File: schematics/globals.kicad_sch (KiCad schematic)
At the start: 20 parts, among them J1 Power, SW1 SW_Push, U1 74HC04, U12 74HC04, U2 NE555P, Y1 4MHz

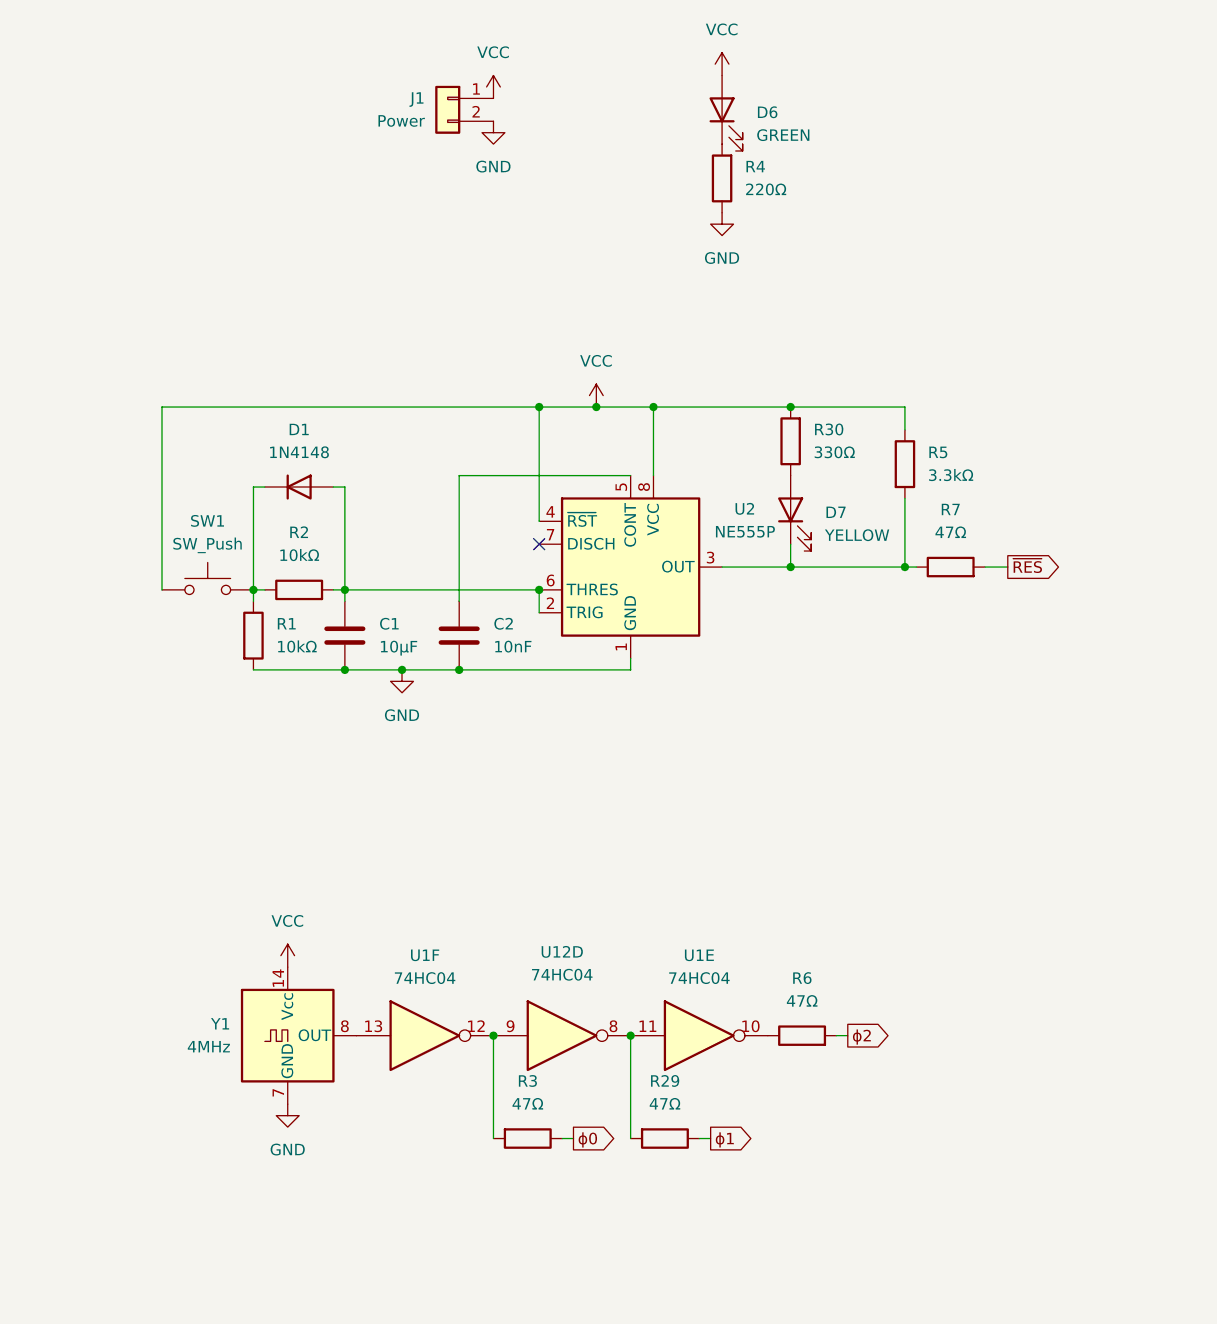
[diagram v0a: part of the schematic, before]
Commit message: trying to make it automatically hold reset during power-on. it's a little better
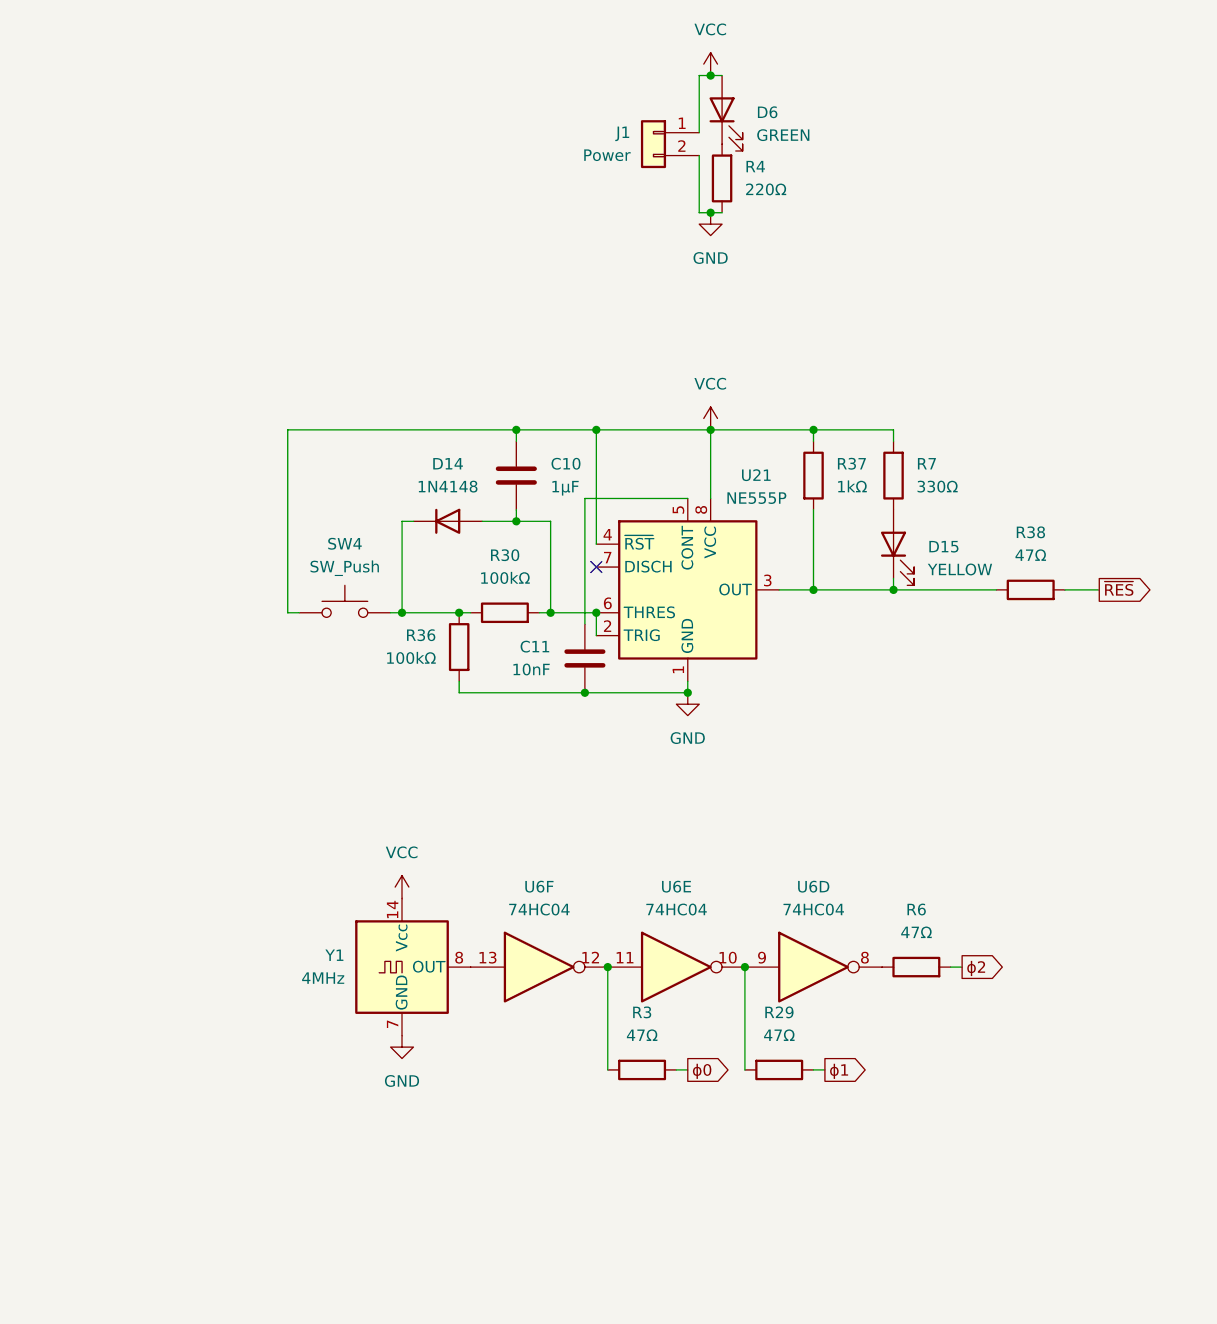
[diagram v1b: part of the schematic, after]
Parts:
- removed C1: 10µF, symbol Device:C
- removed C2: 10nF, symbol Device:C
- removed D1: 1N4148, Diode_THT:D_DO-35_SOD27_P7.62mm_Horizontal, symbol Diode:1N4148
- removed D7: YELLOW, symbol Device:LED
- removed R1, R2: 10kΩ, symbol Device:R
- removed R5: 3.3kΩ, symbol Device:R
- removed SW1: SW_Push, symbol Switch:SW_Push
- removed U2: NE555P, Package_DIP:DIP-8_W7.62mm, symbol Timer:NE555P
- added C10: 1µF, symbol Device:C
- added C11: 10nF, symbol Device:C
- added D14: 1N4148, Diode_THT:D_DO-35_SOD27_P7.62mm_Horizontal, symbol Diode:1N4148
- added D15: YELLOW, symbol Device:LED
- added R36: 100kΩ, symbol Device:R
- added R37: 1kΩ, symbol Device:R
- added R38: 47Ω, symbol Device:R
- added SW4: SW_Push, symbol Switch:SW_Push
- added U21: NE555P, Package_DIP:DIP-8_W7.62mm, symbol Timer:NE555P
- R30: value 330Ω -> 100kΩ
- R7: value 47Ω -> 330Ω
- renumbered U1 to U6, U12 to U6
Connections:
- net GND: now also C11.1, R36.2, U21.1 (GND)
- net VCC: now also R7.2, C10.2, R37.1, SW4.1, U21.4 (~{RST}), U21.8 (VCC); no longer R30.2
- net ~{RES}: now also R38.2; no longer R7.2
- net at R3.2, U6.12: now also U6.11; no longer U6.9
- net at R7.1: now also D15.2 (A)
- net at R6.1: now also U6.8; no longer U6.10
- net at R30.1: now also D14.1 (K), R36.1, SW4.2
- new net: C10.1, D14.2 (A), R30.2, U21.2 (TRIG), U21.6 (THRES)
- new net: D15.1 (K), R37.2, R38.1, U21.3 (OUT)
- new net: R29.2, U6.10, U6.9
- new net: C11.2, U21.5 (CONT)
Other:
- moved on the sheet: J1, R29, R3, R6, U6D, U6E, U6F, Y1

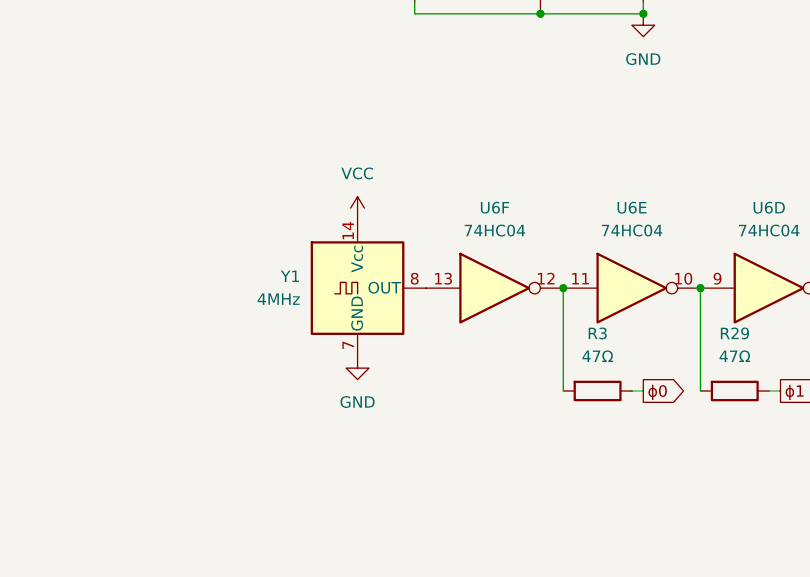
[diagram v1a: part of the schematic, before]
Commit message: removed unnecessary clock inversion
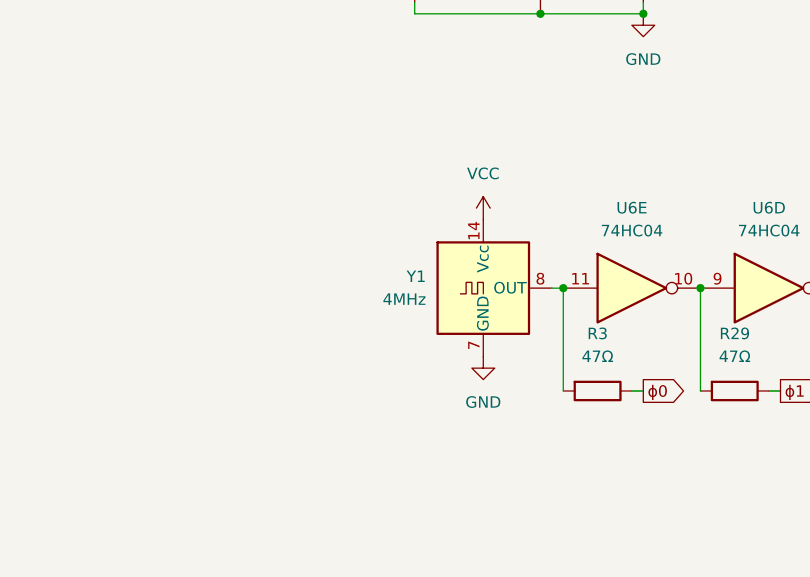
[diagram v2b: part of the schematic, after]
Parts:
- removed unit 6 of U6
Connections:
- net at R3.2, U6.11: now also Y1.8 (OUT)
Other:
- moved on the sheet: Y1
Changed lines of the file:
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@@
+	)
+	(junction
+		(at 143.51 127)
+		(diameter 0)
+		(color 0 0 0 0)
 	)
 	(junction
@@
 	)
 	(junction
-		(at 143.51 127)
-		(diameter 0)
-		(color 0 0 0 0)
-	)
-	(junction
 		(at 158.75 127)
 		(diameter 0)
@@
 		(pts
 			(xy 120.65 77.47) (xy 120.65 87.63)
+		)
+		(stroke
+			(width 0)
+			(type default)
+		)
+	)
+	(wire
+		(pts
+			(xy 142.24 127) (xy 143.51 127)
 		)
 		(stroke
@@
 	)
 	(symbol
-		(lib_id "74xx:74HC04")
-		(at 135.89 127 0)
-		(unit 6)
-		(body_style 1)
-		(exclude_from_sim no)
-		(in_bom yes)
-		(on_board yes)
-		(in_pos_files yes)
-		(dnp no)
-		(fields_autoplaced yes)
-		(property "Reference" "U6"
-			(at 135.89 118.11 0)
-			(show_name no)
-			(do_not_autoplace no)
-			(effects
-				(font
-					(size 1.27 1.27)
-				)
-			)
-		)
-		(property "Value" "74HC04"
-			(at 135.89 120.65 0)
-			(show_name no)
-			(do_not_autoplace no)
-			(effects
-				(font
-					(size 1.27 1.27)
-				)
-			)
-		)
-		(property "Footprint" ""
-			(at 135.89 127 0)
-			(hide yes)
-			(show_name no)
-			(do_not_autoplace no)
-			(effects
-				(font
-					(size 1.27 1.27)
-				)
-			)
-		)
-		(property "Datasheet" "https://assets.nexperia.com/documents/data-sheet/74HC_HCT04.pdf"
-			(at 135.89 127 0)
-			(hide yes)
-			(show_name no)
-			(do_not_autoplace no)
-			(effects
-				(font
-					(size 1.27 1.27)
-				)
-			)
-		)
-		(property "Description" "Hex Inverter"
-			(at 135.89 127 0)
-			(hide yes)
-			(show_name no)
-			(do_not_autoplace no)
-			(effects
-				(font
-					(size 1.27 1.27)
-				)
-			)
-		)
-		(pin "11"
-		)
-		(pin "12"
-		)
-		(pin "14"
-		)
-		(pin "10"
-		)
-		(pin "7"
-		)
-		(pin "13"
-		)
-		(pin "1"
-		)
-		(pin "8"
-		)
-		(pin "2"
-		)
-		(pin "3"
-		)
-		(pin "4"
-		)
-		(pin "5"
-		)
-		(pin "6"
-		)
-		(pin "9"
-		)
-		(instances
-			(project "bv6502_hw"
-				(path "/94c72abe-aaa5-49aa-8ab7-5d3e7cbc10be/560ef1bd-4b3f-459c-9f6a-9898850b3c5b"
-					(reference "U6")
-					(unit 6)
-				)
-			)
-		)
-	)
-	(symbol
 		(lib_id "power:VCC")
 		(at 154.94 27.94 0)
@@
 	(symbol
 		(lib_id "Oscillator:DGOF5S3")
-		(at 120.65 127 0)
+		(at 134.62 127 0)
 		(unit 1)
 		(body_style 1)
@@
 		(fields_autoplaced yes)
 		(property "Reference" "Y1"
-			(at 114.3 125.7299 0)
+			(at 128.27 125.7299 0)
 			(show_name no)
 			(do_not_autoplace no)
@@
 		)
 		(property "Value" "4MHz"
-			(at 114.3 128.2699 0)
+			(at 128.27 128.2699 0)
 			(show_name no)
 			(do_not_autoplace no)
@@
 		)
 		(property "Footprint" "Oscillator:Oscillator_DIP-14"
-			(at 132.08 135.89 0)
+			(at 146.05 135.89 0)
 			(hide yes)
 			(show_name no)
@@
 		)
 		(property "Datasheet" "http://www.conwin.com/datasheets/cx/cx030.pdf"
-			(at 118.11 127 0)
+			(at 132.08 127 0)
 			(hide yes)
 			(show_name no)
@@
 		)
 		(property "Description" "HCMOS Crystal Clock Oscillator, DIP14-style metal package"
-			(at 120.65 127 0)
+			(at 134.62 127 0)
 			(hide yes)
 			(show_name no)
@@
 	(symbol
 		(lib_id "power:VCC")
-		(at 120.65 119.38 0)
+		(at 134.62 119.38 0)
 		(unit 1)
 		(body_style 1)
@@
 		(fields_autoplaced yes)
 		(property "Reference" "#PWR03"
-			(at 120.65 123.19 0)
+			(at 134.62 123.19 0)
 			(hide yes)
 			(show_name no)
@@
 		)
 		(property "Value" "VCC"
-			(at 120.65 114.3 0)
+			(at 134.62 114.3 0)
 			(show_name no)
 			(do_not_autoplace no)
@@
 		)
 		(property "Footprint" ""
-			(at 120.65 119.38 0)
+			(at 134.62 119.38 0)
 			(hide yes)
 			(show_name no)
@@
 		)
 		(property "Datasheet" ""
-			(at 120.65 119.38 0)
+			(at 134.62 119.38 0)
 			(hide yes)
 			(show_name no)
@@
 		)
 		(property "Description" "Power symbol creates a global label with name \"VCC\""
-			(at 120.65 119.38 0)
+			(at 134.62 119.38 0)
 			(hide yes)
 			(show_name no)
@@
 	(symbol
 		(lib_id "power:GND")
-		(at 120.65 134.62 0)
+		(at 134.62 134.62 0)
 		(unit 1)
 		(body_style 1)
@@
 		(fields_autoplaced yes)
 		(property "Reference" "#PWR04"
-			(at 120.65 140.97 0)
+			(at 134.62 140.97 0)
 			(hide yes)
 			(show_name no)
@@
 		)
 		(property "Value" "GND"
-			(at 120.65 139.7 0)
+			(at 134.62 139.7 0)
 			(show_name no)
 			(do_not_autoplace no)
@@
 		)
 		(property "Footprint" ""
-			(at 120.65 134.62 0)
+			(at 134.62 134.62 0)
 			(hide yes)
 			(show_name no)
@@
 		)
 		(property "Datasheet" ""
-			(at 120.65 134.62 0)
+			(at 134.62 134.62 0)
 			(hide yes)
 			(show_name no)
@@
 		)
 		(property "Description" "Power symbol creates a global label with name \"GND\" , ground"
-			(at 120.65 134.62 0)
-			(hide yes)
-			(show_name no)
+			(at 134.62 134.62 0)
+			(hide yes)
+			(show_name no)

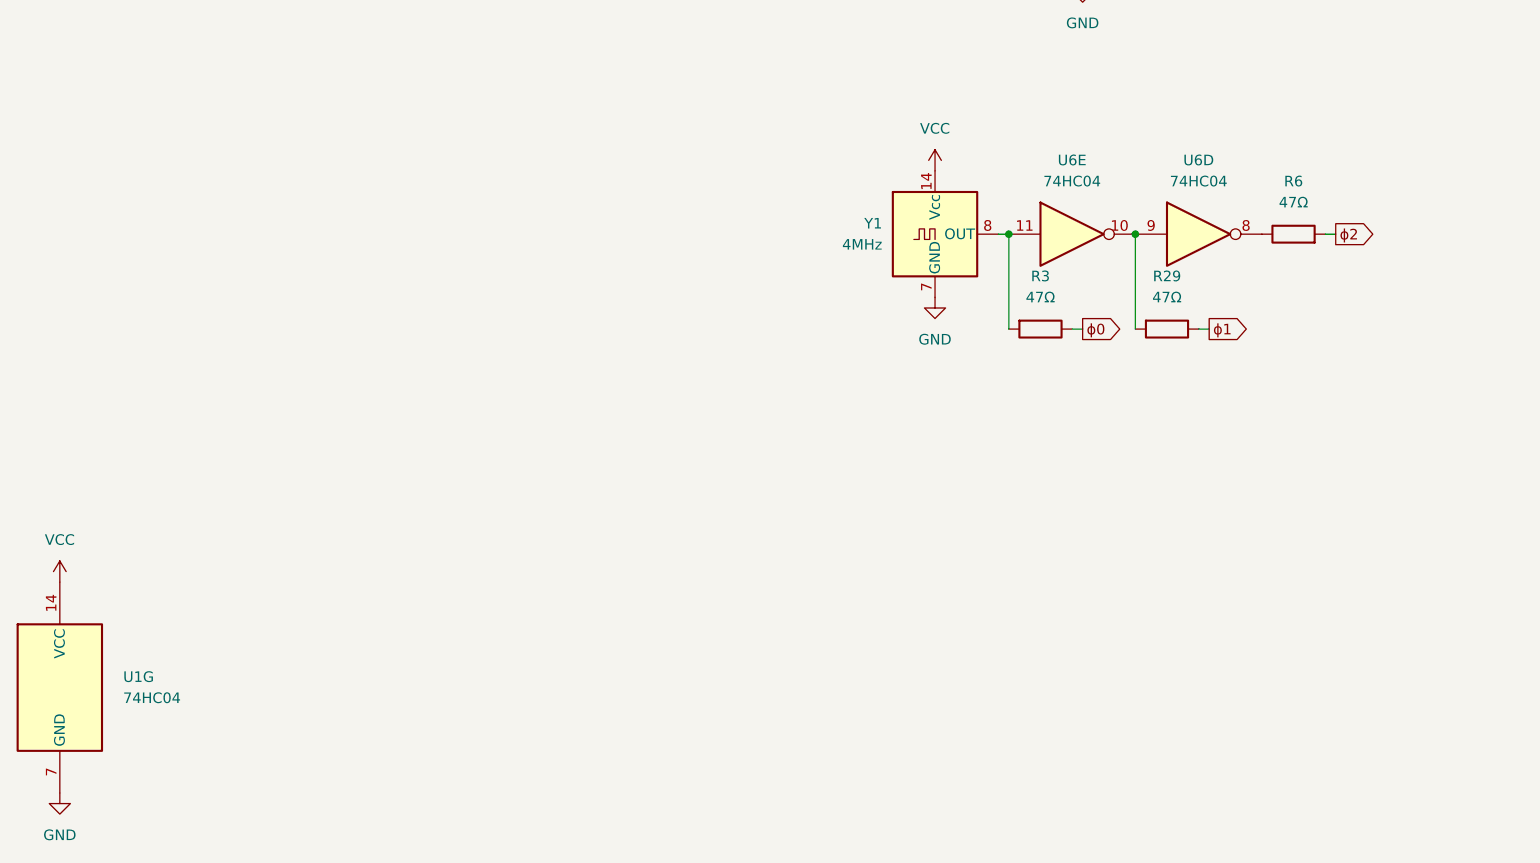
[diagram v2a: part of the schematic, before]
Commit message: Address decoder pld file and no-VIA keyboard schematic and pld file.
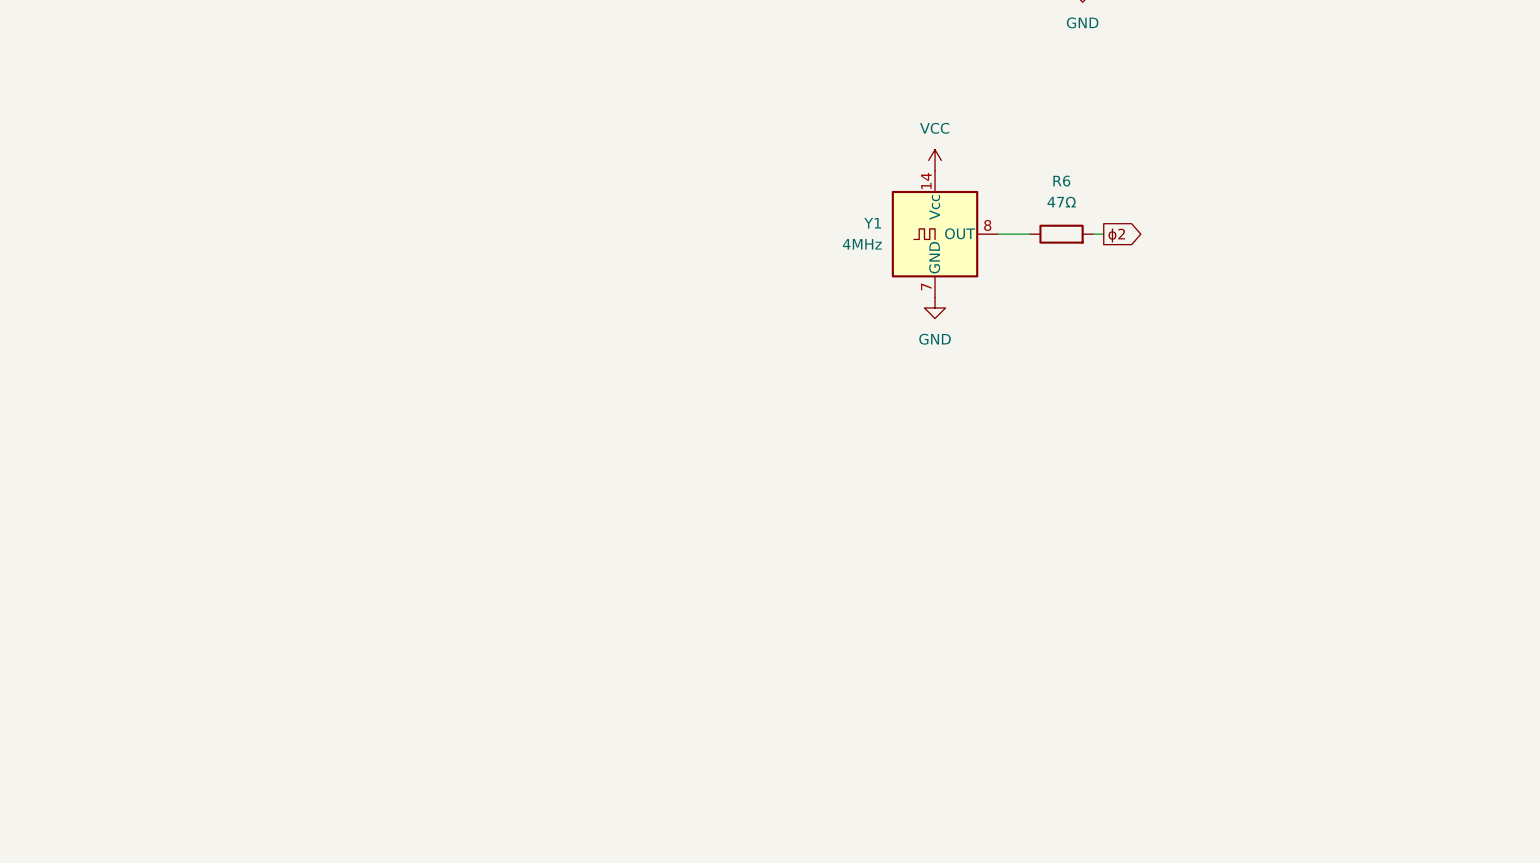
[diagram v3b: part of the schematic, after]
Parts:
- removed R29, R3: 47Ω, symbol Device:R
- removed U1, U6: 74HC04, symbol 74xx:74HC04
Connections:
- net at Y1.8 (OUT): now also R6.1
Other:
- moved on the sheet: R6
